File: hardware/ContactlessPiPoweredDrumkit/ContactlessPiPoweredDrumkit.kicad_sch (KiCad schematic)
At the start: 12 parts, among them J1 Raspberry_Pi_1_2_3, U1 SN74LVC1T45DCK

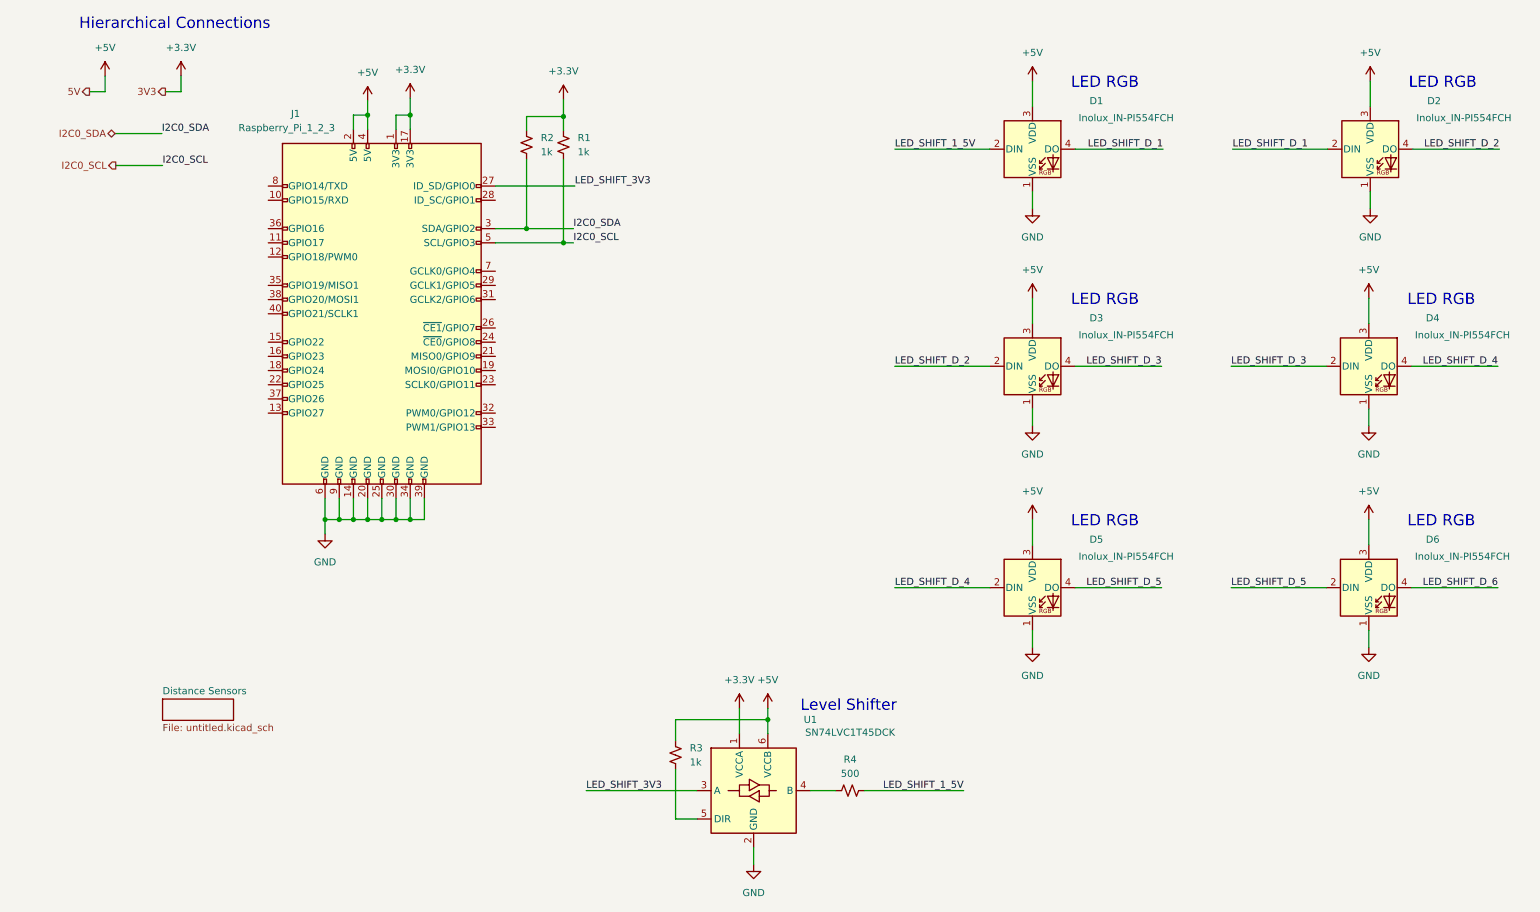
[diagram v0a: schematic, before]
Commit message: Add Hierarchical Connections and Distance Sensors
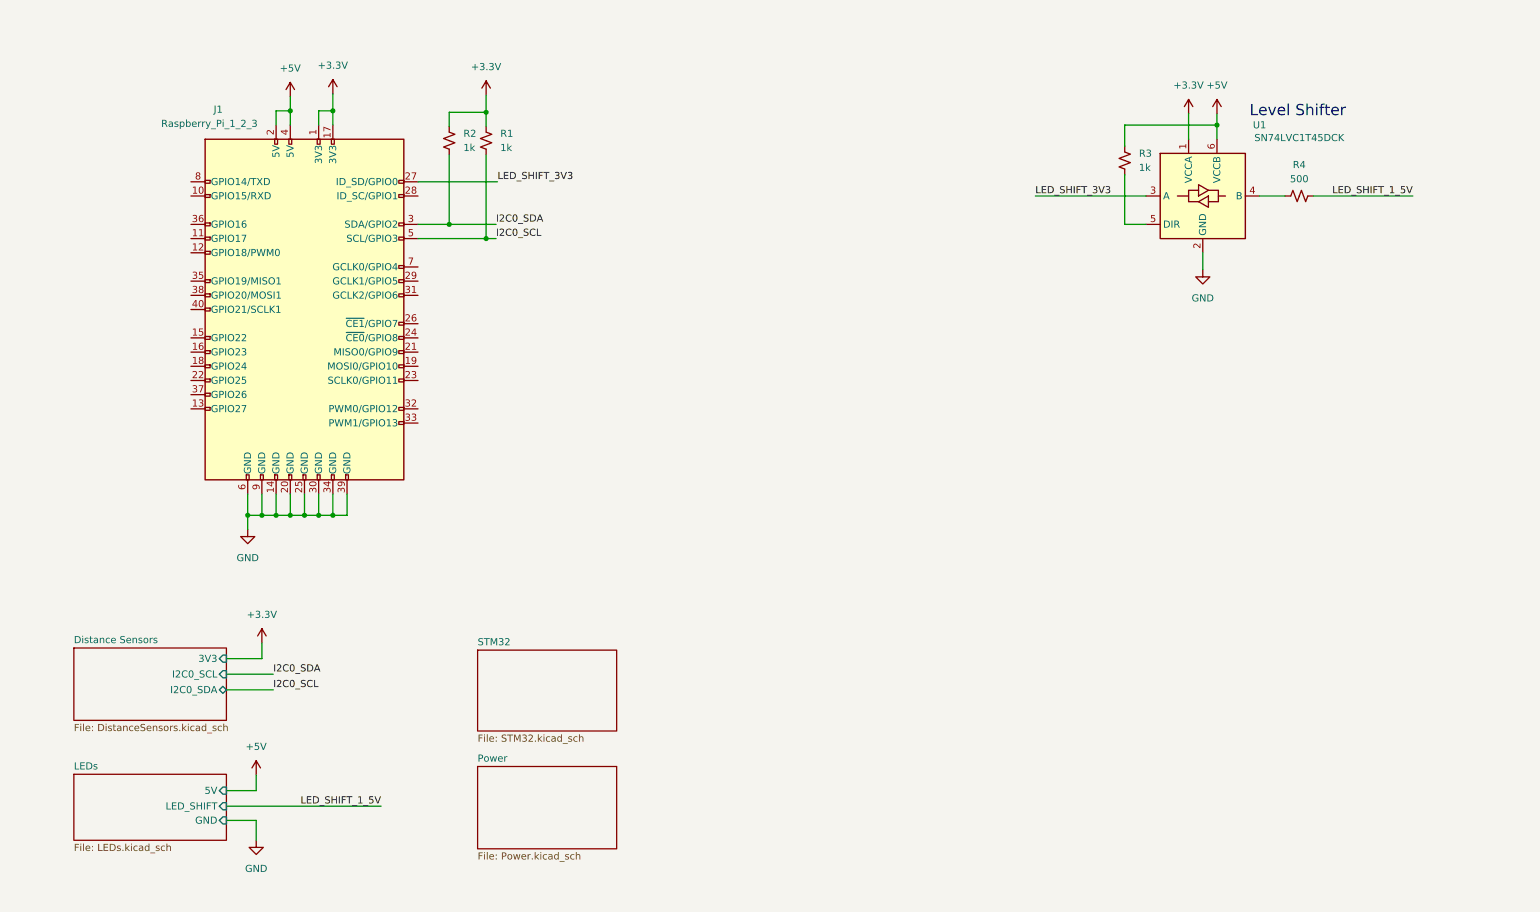
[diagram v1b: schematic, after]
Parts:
- removed D1, D2, D3, D4, D5, D6: Inolux_IN-PI554FCH, LED_SMD:LED_Inolux_IN-PI554FCH_PLCC4_5.0x5.0mm_P3.2mm, symbol LED:Inolux_IN-PI554FCH
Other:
- added sheet LEDs (LEDs.kicad_sch)
- added sheet Power (Power.kicad_sch)
- added sheet STM32 (STM32.kicad_sch)
- sheet Distance Sensors: file untitled.kicad_sch -> DistanceSensors.kicad_sch
- sheet Distance Sensors ports: added 3V3, I2C0_SCL, I2C0_SDA; removed none
- note removed: "Hierarchical Connections"
- note removed: "LED RGB"
- title: (none) -> RPI and Root
- moved on the sheet: J1, R1, R2, R3, R4, U1

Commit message: Update Hierarchy Page
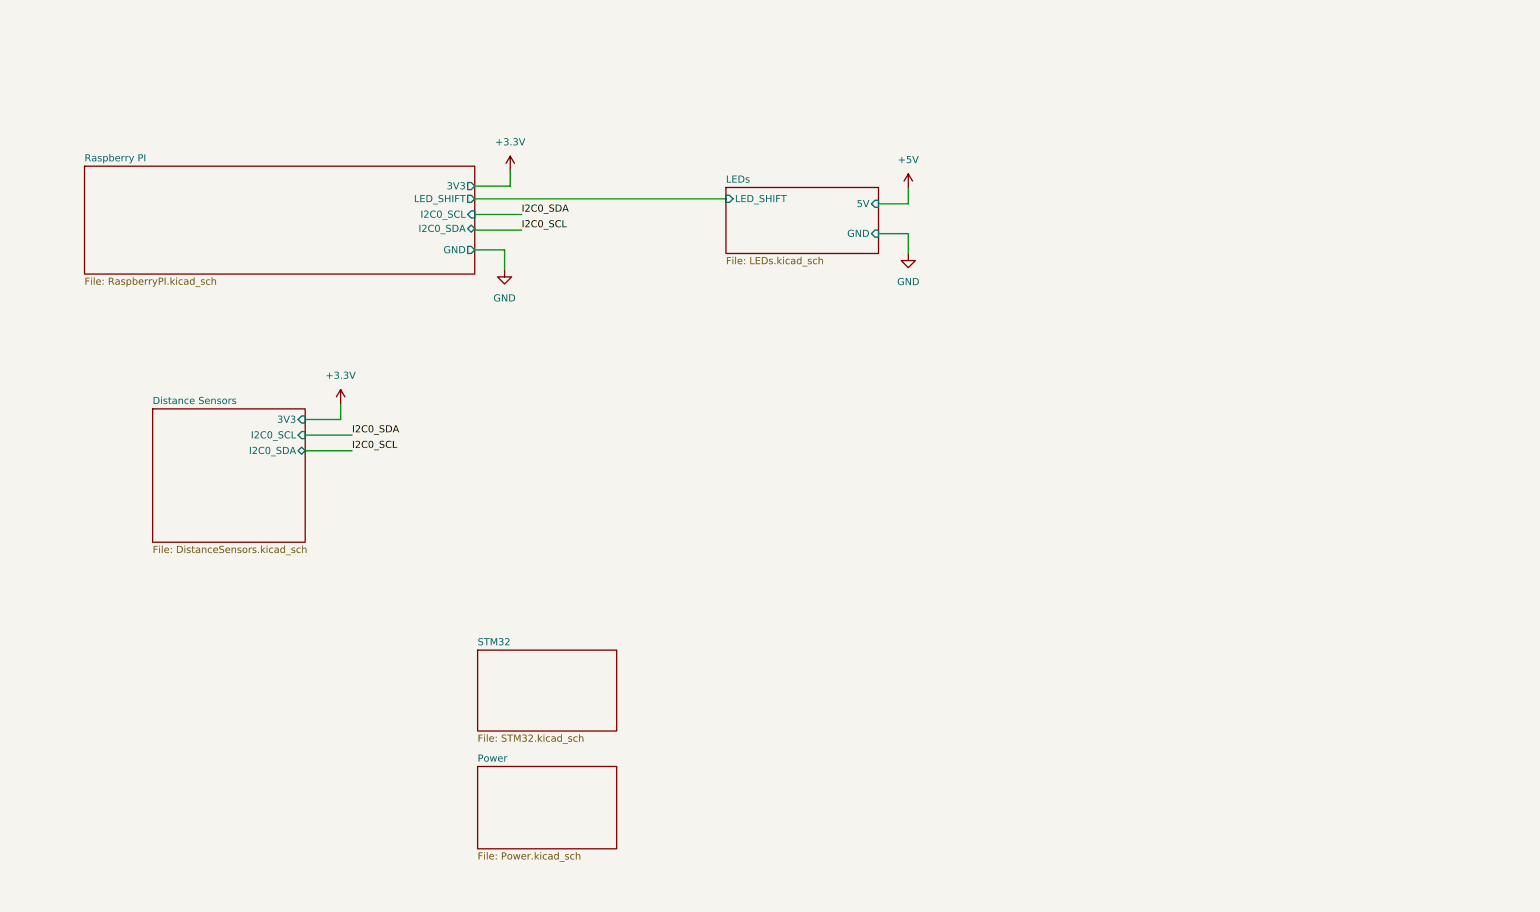
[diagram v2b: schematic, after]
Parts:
- removed J1: Raspberry_Pi_1_2_3, Connector_PinSocket_2.54mm:PinSocket_2x20_P2.54mm_Vertical, symbol Connector:Raspberry_Pi_2_3
- removed R1, R2, R3: 1k, symbol Device:R_Small_US
- removed R4: 500, symbol Device:R_Small_US
- removed U1: SN74LVC1T45DCK, Package_TO_SOT_SMD:SOT-363_SC-70-6, symbol Logic_LevelTranslator:SN74LVC1T45DCK
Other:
- added sheet Raspberry PI (RaspberryPI.kicad_sch)
- note removed: "Level Shifter"
- title: RPI and Root -> Hierarchy

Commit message: Complete PCB Layout
Completed PCB layout
Custom Artwork
Generate Gerbers
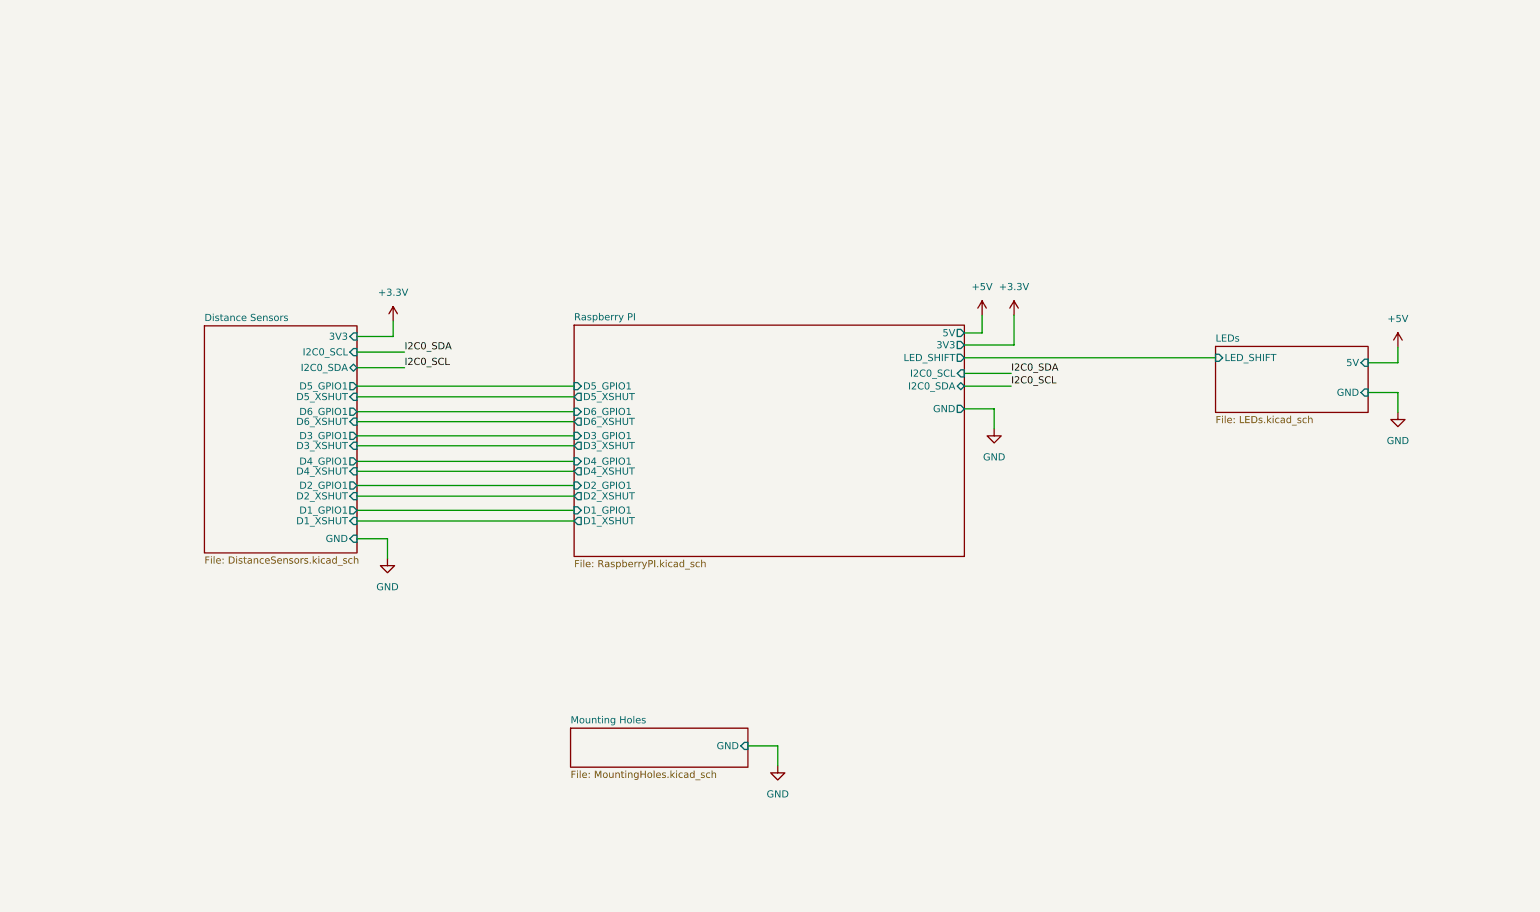
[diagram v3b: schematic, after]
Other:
- removed sheet Power
- removed sheet STM32
- added sheet Mounting Holes (MountingHoles.kicad_sch)
- sheet Distance Sensors ports: added D1_GPIO1, D1_XSHUT, D2_GPIO1, D2_XSHUT, D3_GPIO1, D3_XSHUT, D4_GPIO1, D4_XSHUT, D5_GPIO1, D5_XSHUT, D6_GPIO1, D6_XSHUT, GND; removed none
- sheet Raspberry PI ports: added 5V, D1_GPIO1, D1_XSHUT, D2_GPIO1, D2_XSHUT, D3_GPIO1, D3_XSHUT, D4_GPIO1, D4_XSHUT, D5_GPIO1, D5_XSHUT, D6_GPIO1, D6_XSHUT; removed none
